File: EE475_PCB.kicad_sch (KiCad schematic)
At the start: 13 parts, among them J1 Conn_01x15_Female, J2 Conn_01x02_Female, J3 Conn_01x15_Female, J4 Conn_01x02_Female, J5 Conn_01x02_Female, J6 Conn_01x02_Female, J7 Conn_01x02_Female, J8 Conn_01x02_Female, Q1 S8050, Q2 S8050

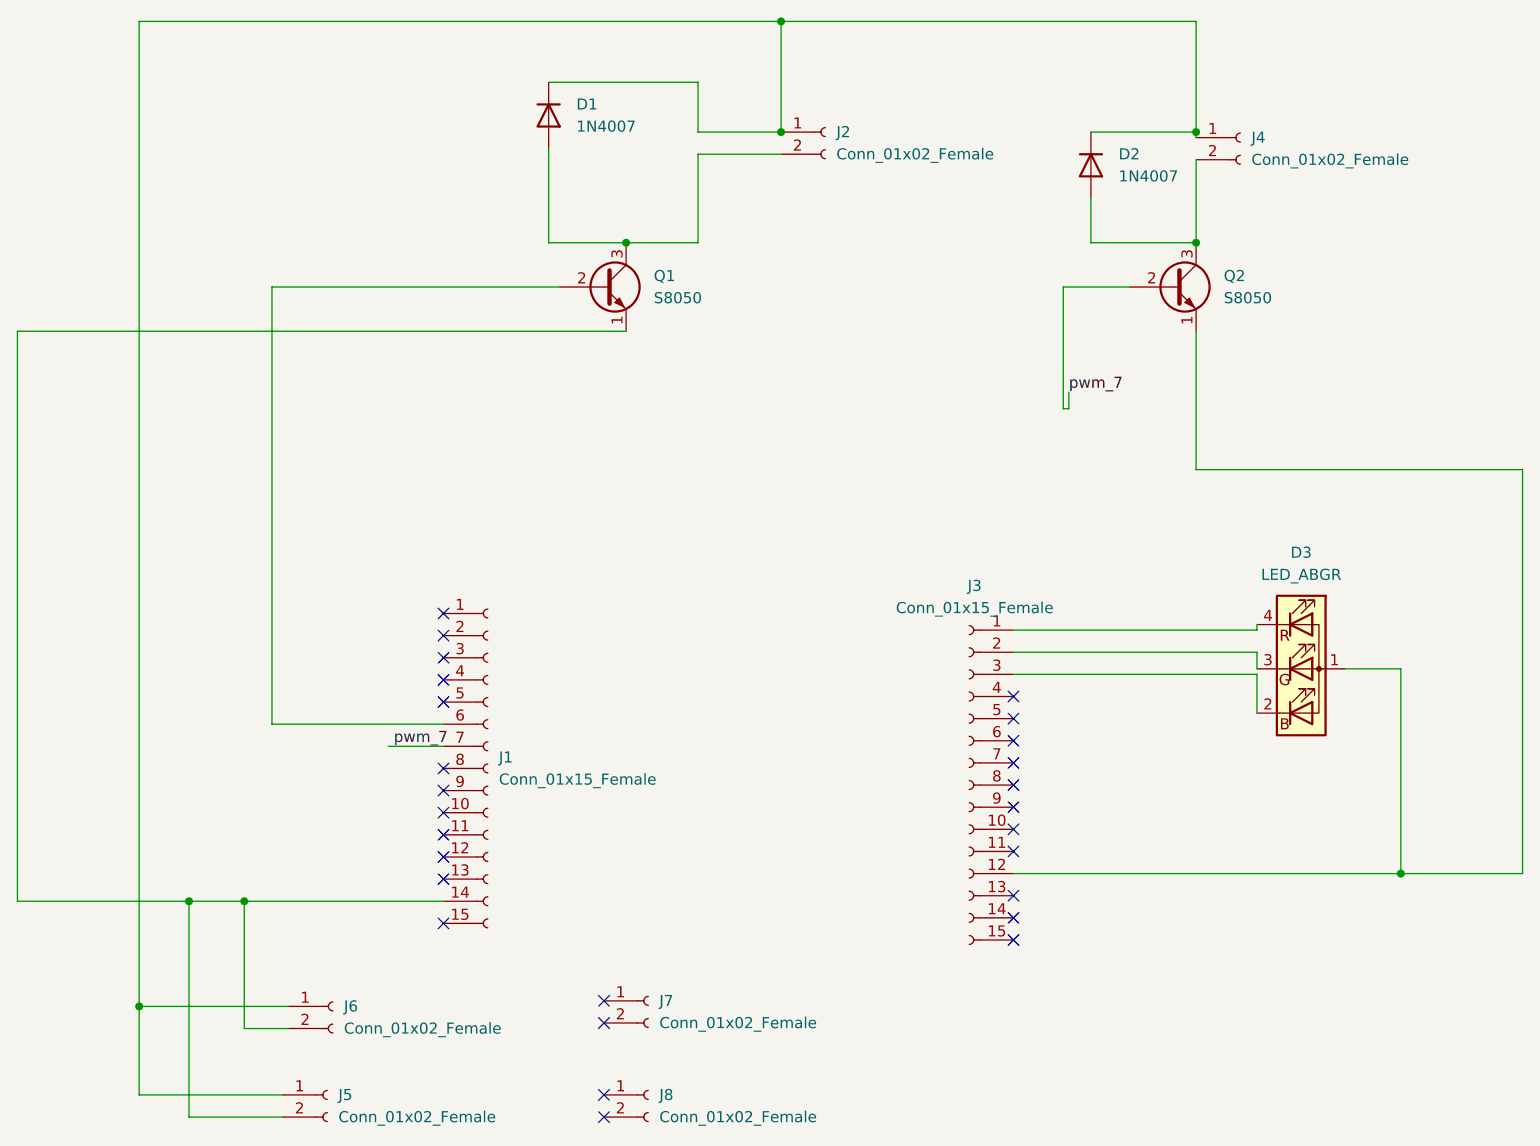
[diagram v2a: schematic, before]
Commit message: Updated version of the PCB based on professor and TAs feedback
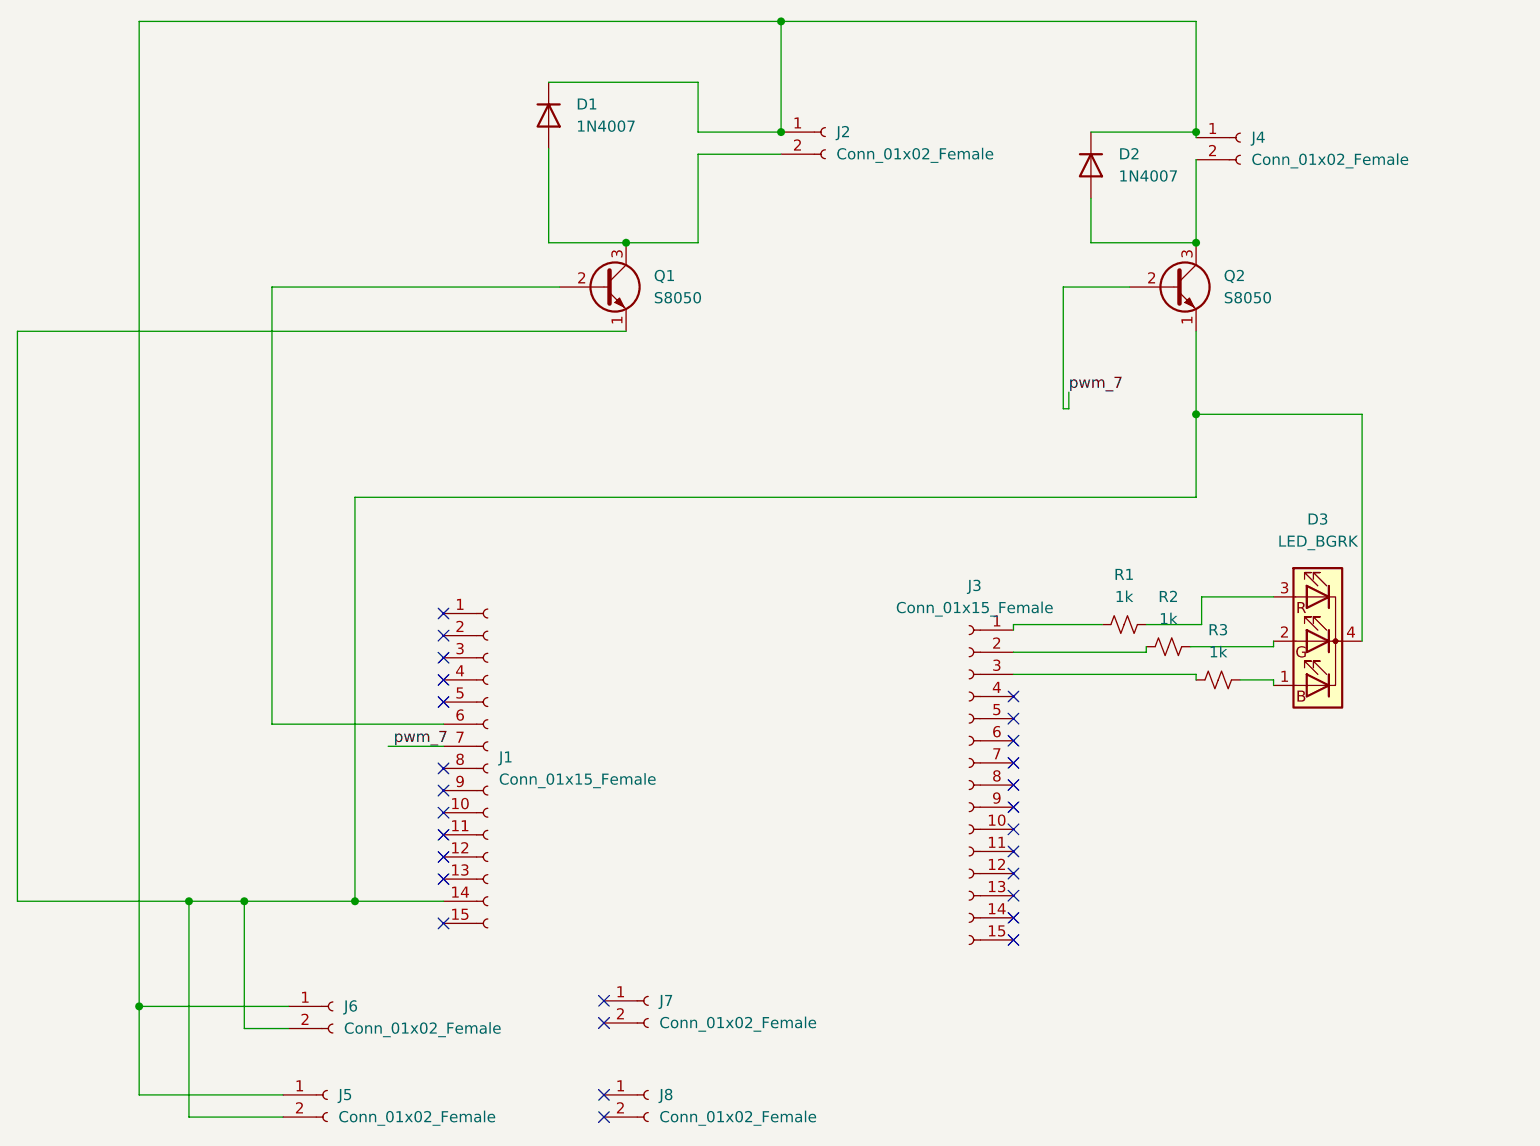
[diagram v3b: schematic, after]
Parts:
- removed D3: LED_ABGR, LED_SMD:LED_RGB_1210, symbol Device:LED_ABGR
- added D3: LED_BGRK, LED_SMD:LED_RGB_1210, symbol Device:LED_BGRK
- added R1, R2, R3: 1k, Resistor_SMD:R_0402_1005Metric, symbol Device:R_Small_US
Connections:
- net at J1.14 (Pin_14), J5.2 (Pin_2), J6.2 (Pin_2)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: now also Q2.1 (E), D3.4 (K)
- net at J3.12 (Pin_12): no longer Q2.1 (E)
- net at J3.3 (Pin_3): now also R3.2
- net at J3.2 (Pin_2): now also R2.2
- net at J3.1 (Pin_1): now also R1.2
- new net: D3.2 (GA), R2.1
- new net: D3.3 (RA), R1.1
- new net: D3.1 (BA), R3.1
- no-connect marks 27 -> 28
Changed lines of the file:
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@@
   (junction (at 73.025 138.43) (diameter 0) (color 0 0 0 0)
   )
+  (junction (at 194.31 70.485) (diameter 0) (color 0 0 0 0)
+  )
+  (junction (at 97.79 126.365) (diameter 0) (color 0 0 0 0)
+  )
   (junction (at 194.31 38.1) (diameter 0) (color 0 0 0 0)
-  )
-  (junction (at 217.805 123.19) (diameter 0) (color 0 0 0 0)
   )
   (junction (at 146.685 25.4) (diameter 0) (color 0 0 0 0)
@@
   (no_connect (at 107.95 113.665))
   (no_connect (at 173.355 102.87))
+  (no_connect (at 173.355 123.19))
   (no_connect (at 107.95 95.885))
   (no_connect (at 173.355 128.27))
@@
   (no_connect (at 107.95 116.205))
   (no_connect (at 107.95 93.345))
-  (wire (pts (xy 231.775 123.19) (xy 217.805 123.19))
-    (stroke (width 0) (type default) (color 0 0 0 0))
-  )
-  (wire (pts (xy 231.775 76.835) (xy 231.775 123.19))
+  (wire (pts (xy 173.355 94.615) (xy 173.355 95.25))
+    (stroke (width 0) (type default) (color 0 0 0 0))
+  )
+  (wire (pts (xy 97.79 80.01) (xy 97.79 126.365))
     (stroke (width 0) (type default) (color 0 0 0 0))
   )
@@
     (stroke (width 0) (type default) (color 0 0 0 0))
   )
+  (wire (pts (xy 199.39 100.965) (xy 203.2 100.965))
+    (stroke (width 0) (type default) (color 0 0 0 0))
+  )
+  (wire (pts (xy 203.2 100.965) (xy 203.2 101.6))
+    (stroke (width 0) (type default) (color 0 0 0 0))
+  )
   (wire (pts (xy 146.685 25.4) (xy 73.025 25.4))
     (stroke (width 0) (type default) (color 0 0 0 0))
@@
     (stroke (width 0) (type default) (color 0 0 0 0))
   )
-  (wire (pts (xy 194.31 76.835) (xy 231.775 76.835))
-    (stroke (width 0) (type default) (color 0 0 0 0))
-  )
   (wire (pts (xy 59.055 126.365) (xy 59.055 60.96))
     (stroke (width 0) (type default) (color 0 0 0 0))
   )
+  (wire (pts (xy 188.595 94.615) (xy 194.945 94.615))
+    (stroke (width 0) (type default) (color 0 0 0 0))
+  )
   (wire (pts (xy 179.705 67.945) (xy 179.705 69.85))
     (stroke (width 0) (type default) (color 0 0 0 0))
@@
     (stroke (width 0) (type default) (color 0 0 0 0))
   )
-  (wire (pts (xy 173.355 100.33) (xy 201.295 100.33))
+  (wire (pts (xy 194.31 80.01) (xy 97.79 80.01))
+    (stroke (width 0) (type default) (color 0 0 0 0))
+  )
+  (wire (pts (xy 194.945 91.44) (xy 203.2 91.44))
     (stroke (width 0) (type default) (color 0 0 0 0))
   )
@@
     (stroke (width 0) (type default) (color 0 0 0 0))
   )
-  (wire (pts (xy 201.295 99.695) (xy 201.295 97.79))
+  (wire (pts (xy 183.515 94.615) (xy 173.355 94.615))
+    (stroke (width 0) (type default) (color 0 0 0 0))
+  )
+  (wire (pts (xy 188.595 97.79) (xy 188.595 97.155))
+    (stroke (width 0) (type default) (color 0 0 0 0))
+  )
+  (wire (pts (xy 213.36 96.52) (xy 213.36 70.485))
     (stroke (width 0) (type default) (color 0 0 0 0))
   )
@@
     (stroke (width 0) (type default) (color 0 0 0 0))
   )
-  (wire (pts (xy 217.805 123.19) (xy 173.355 123.19))
-    (stroke (width 0) (type default) (color 0 0 0 0))
-  )
   (wire (pts (xy 73.025 25.4) (xy 73.025 138.43))
     (stroke (width 0) (type default) (color 0 0 0 0))
@@
     (stroke (width 0) (type default) (color 0 0 0 0))
   )
-  (wire (pts (xy 173.355 95.25) (xy 201.295 95.25))
-    (stroke (width 0) (type default) (color 0 0 0 0))
-  )
   (wire (pts (xy 194.31 25.4) (xy 146.685 25.4))
     (stroke (width 0) (type default) (color 0 0 0 0))
@@
     (stroke (width 0) (type default) (color 0 0 0 0))
   )
-  (wire (pts (xy 201.295 97.79) (xy 173.355 97.79))
+  (wire (pts (xy 173.355 97.79) (xy 188.595 97.79))
     (stroke (width 0) (type default) (color 0 0 0 0))
   )
@@
     (stroke (width 0) (type default) (color 0 0 0 0))
   )
-  (wire (pts (xy 201.295 100.33) (xy 201.295 104.775))
+  (wire (pts (xy 193.675 97.155) (xy 203.2 97.155))
+    (stroke (width 0) (type default) (color 0 0 0 0))
+  )
+  (wire (pts (xy 97.79 126.365) (xy 85.09 126.365))
+    (stroke (width 0) (type default) (color 0 0 0 0))
+  )
+  (wire (pts (xy 194.945 94.615) (xy 194.945 91.44))
     (stroke (width 0) (type default) (color 0 0 0 0))
   )
@@
     (stroke (width 0) (type default) (color 0 0 0 0))
   )
-  (wire (pts (xy 194.31 60.96) (xy 194.31 76.835))
-    (stroke (width 0) (type default) (color 0 0 0 0))
-  )
-  (wire (pts (xy 201.295 95.25) (xy 201.295 94.615))
+  (wire (pts (xy 194.31 60.96) (xy 194.31 70.485))
     (stroke (width 0) (type default) (color 0 0 0 0))
   )
@@
     (stroke (width 0) (type default) (color 0 0 0 0))
   )
+  (wire (pts (xy 194.31 100.33) (xy 194.31 100.965))
+    (stroke (width 0) (type default) (color 0 0 0 0))
+  )
   (wire (pts (xy 89.535 151.13) (xy 78.74 151.13))
     (stroke (width 0) (type default) (color 0 0 0 0))
   )
-  (wire (pts (xy 211.455 99.695) (xy 217.805 99.695))
-    (stroke (width 0) (type default) (color 0 0 0 0))
-  )
-  (wire (pts (xy 107.95 126.365) (xy 85.09 126.365))
+  (wire (pts (xy 107.95 126.365) (xy 97.79 126.365))
+    (stroke (width 0) (type default) (color 0 0 0 0))
+  )
+  (wire (pts (xy 194.31 70.485) (xy 194.31 80.01))
     (stroke (width 0) (type default) (color 0 0 0 0))
   )
@@
     (stroke (width 0) (type default) (color 0 0 0 0))
   )
+  (wire (pts (xy 203.2 97.155) (xy 203.2 96.52))
+    (stroke (width 0) (type default) (color 0 0 0 0))
+  )
+  (wire (pts (xy 173.355 100.33) (xy 194.31 100.33))
+    (stroke (width 0) (type default) (color 0 0 0 0))
+  )
   (wire (pts (xy 146.685 40.64) (xy 137.16 40.64))
     (stroke (width 0) (type default) (color 0 0 0 0))
   )
+  (wire (pts (xy 213.36 70.485) (xy 194.31 70.485))
+    (stroke (width 0) (type default) (color 0 0 0 0))
+  )
   (wire (pts (xy 101.6 108.585) (xy 107.95 108.585))
     (stroke (width 0) (type default) (color 0 0 0 0))
   )
   (wire (pts (xy 182.245 45.72) (xy 182.245 50.8))
-    (stroke (width 0) (type default) (color 0 0 0 0))
-  )
-  (wire (pts (xy 217.805 99.695) (xy 217.805 123.19))
     (stroke (width 0) (type default) (color 0 0 0 0))
   )
@@
     )
     (property "Datasheet" "~" (id 3) (at 131.445 148.59 0)
+      (effects (font (size 1.27 1.27)) hide)
+    )
+    (pin "1")
+    (pin "2")
+  )
+  (symbol (lib_id "Device:R_Small_US") (at 191.135 97.155 270) (unit 1)
+    (in_bom yes) (on_board yes) (fields_autoplaced)
+    (property "Reference" "R2" (id 0) (at 191.135 91.44 90))
+    (property "Value" "1k" (id 1) (at 191.135 93.98 90))
+    (property "Footprint" "Resistor_SMD:R_0402_1005Metric" (id 2) (at 191.135 97.155 0)
+      (effects (font (size 1.27 1.27)) hide)
+    )
+    (property "Datasheet" "~" (id 3) (at 191.135 97.155 0)
+      (effects (font (size 1.27 1.27)) hide)
+    )
+    (pin "1")
+    (pin "2")
+  )
+  (symbol (lib_id "Device:R_Small_US") (at 186.055 94.615 270) (unit 1)
+    (in_bom yes) (on_board yes) (fields_autoplaced)
+    (property "Reference" "R1" (id 0) (at 186.055 88.9 90))
+    (property "Value" "1k" (id 1) (at 186.055 91.44 90))
+    (property "Footprint" "Resistor_SMD:R_0402_1005Metric" (id 2) (at 186.055 94.615 0)
+      (effects (font (size 1.27 1.27)) hide)
+    )
+    (property "Datasheet" "~" (id 3) (at 186.055 94.615 0)
       (effects (font (size 1.27 1.27)) hide)
     )
@@
     (pin "2")
   )
-  (symbol (lib_id "Device:LED_ABGR") (at 206.375 99.695 0) (unit 1)
-    (in_bom yes) (on_board yes) (fields_autoplaced)
-    (property "Reference" "D3" (id 0) (at 206.375 86.36 0))
-    (property "Value" "LED_ABGR" (id 1) (at 206.375 88.9 0))
-    (property "Footprint" "LED_SMD:LED_RGB_1210" (id 2) (at 206.375 100.965 0)
-      (effects (font (size 1.27 1.27)) hide)
-    )
-    (property "Datasheet" "~" (id 3) (at 206.375 100.965 0)
-      (effects (font (size 1.27 1.27)) hide)
-    )
-    (pin "1")
-    (pin "2")
-    (pin "3")
-    (pin "4")
-  )
   (symbol (lib_id "Connector:Conn_01x02_Female") (at 131.445 137.795 0) (unit 1)
     (in_bom yes) (on_board yes) (fields_autoplaced)
@@
     (pin "3")
   )
+  (symbol (lib_id "Device:LED_BGRK") (at 208.28 96.52 0) (mirror y) (unit 1)
+    (in_bom yes) (on_board yes) (fields_autoplaced)
+    (property "Reference" "D3" (id 0) (at 208.28 82.55 0))
+    (property "Value" "LED_BGRK" (id 1) (at 208.28 85.09 0))
+    (property "Footprint" "LED_SMD:LED_RGB_1210" (id 2) (at 208.28 97.79 0)
+      (effects (font (size 1.27 1.27)) hide)
+    )
+    (property "Datasheet" "~" (id 3) (at 208.28 97.79 0)
+      (effects (font (size 1.27 1.27)) hide)
+    )
+    (pin "1")
+    (pin "2")
+    (pin "3")
+    (pin "4")
+  )
+  (symbol (lib_id "Device:R_Small_US") (at 196.85 100.965 270) (unit 1)
+    (in_bom yes) (on_board yes) (fields_autoplaced)
+    (property "Reference" "R3" (id 0) (at 196.85 95.25 90))
+    (property "Value" "1k" (id 1) (at 196.85 97.79 90))
+    (property "Footprint" "Resistor_SMD:R_0402_1005Metric" (id 2) (at 196.85 100.965 0)
+      (effects (font (size 1.27 1.27)) hide)
+    )
+    (property "Datasheet" "~" (id 3) (at 196.85 100.965 0)
+      (effects (font (size 1.27 1.27)) hide)
+    )
+    (pin "1")
+    (pin "2")
+  )
   (sheet_instances
     (path "/" (page "1"))
@@
       (reference "D2") (unit 1) (value "1N4007") (footprint "Diode_THT:D_DO-41_SOD81_P10.16mm_Horizontal")
     )
-    (path "/bf7f0120-09a6-4dfb-a6a0-88f7d687dcd4"
-      (reference "D3") (unit 1) (value "LED_ABGR") (footprint "LED_SMD:LED_RGB_1210")
+    (path "/dcd044fc-a554-401a-b772-5418f9b2ea05"
+      (reference "D3") (unit 1) (value "LED_BGRK") (footprint "LED_SMD:LED_RGB_1210")
     )
     (path "/5f1a4039-9dd3-4da9-ba86-1190356554ff"
@@
       (reference "Q2") (unit 1) (value "S8050") (footprint "Package_TO_SOT_THT:TO-92_Inline")
     )
-  )
+    (path "/1fa34a24-9490-47ea-9f6f-3b46a7521208"
+      (reference "R1") (unit 1) (value "1k") (footprint "Resistor_SMD:R_0402_1005Metric")
+    )
+    (path "/159d42a8-6e73-481f-bf76-fc0977179af5"
+      (reference "R2") (unit 1) (value "1k") (footprint "Resistor_SMD:R_0402_1005Metric")
+    )
+    (path "/e39de572-5374-4de1-ac89-4ccec206d5ac"
+      (reference "R3") (unit 1) (value "1k") (footprint "Resistor_SMD:R_0402_1005Metric")
+    )
+  )
